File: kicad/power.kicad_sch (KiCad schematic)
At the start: 67 parts, among them J6 RTC Battery, U1 MIMXRT1171DVMAB, U8 TPS62086, U9 TPS62825, Y3 24MHz, Y4 32.768kHz

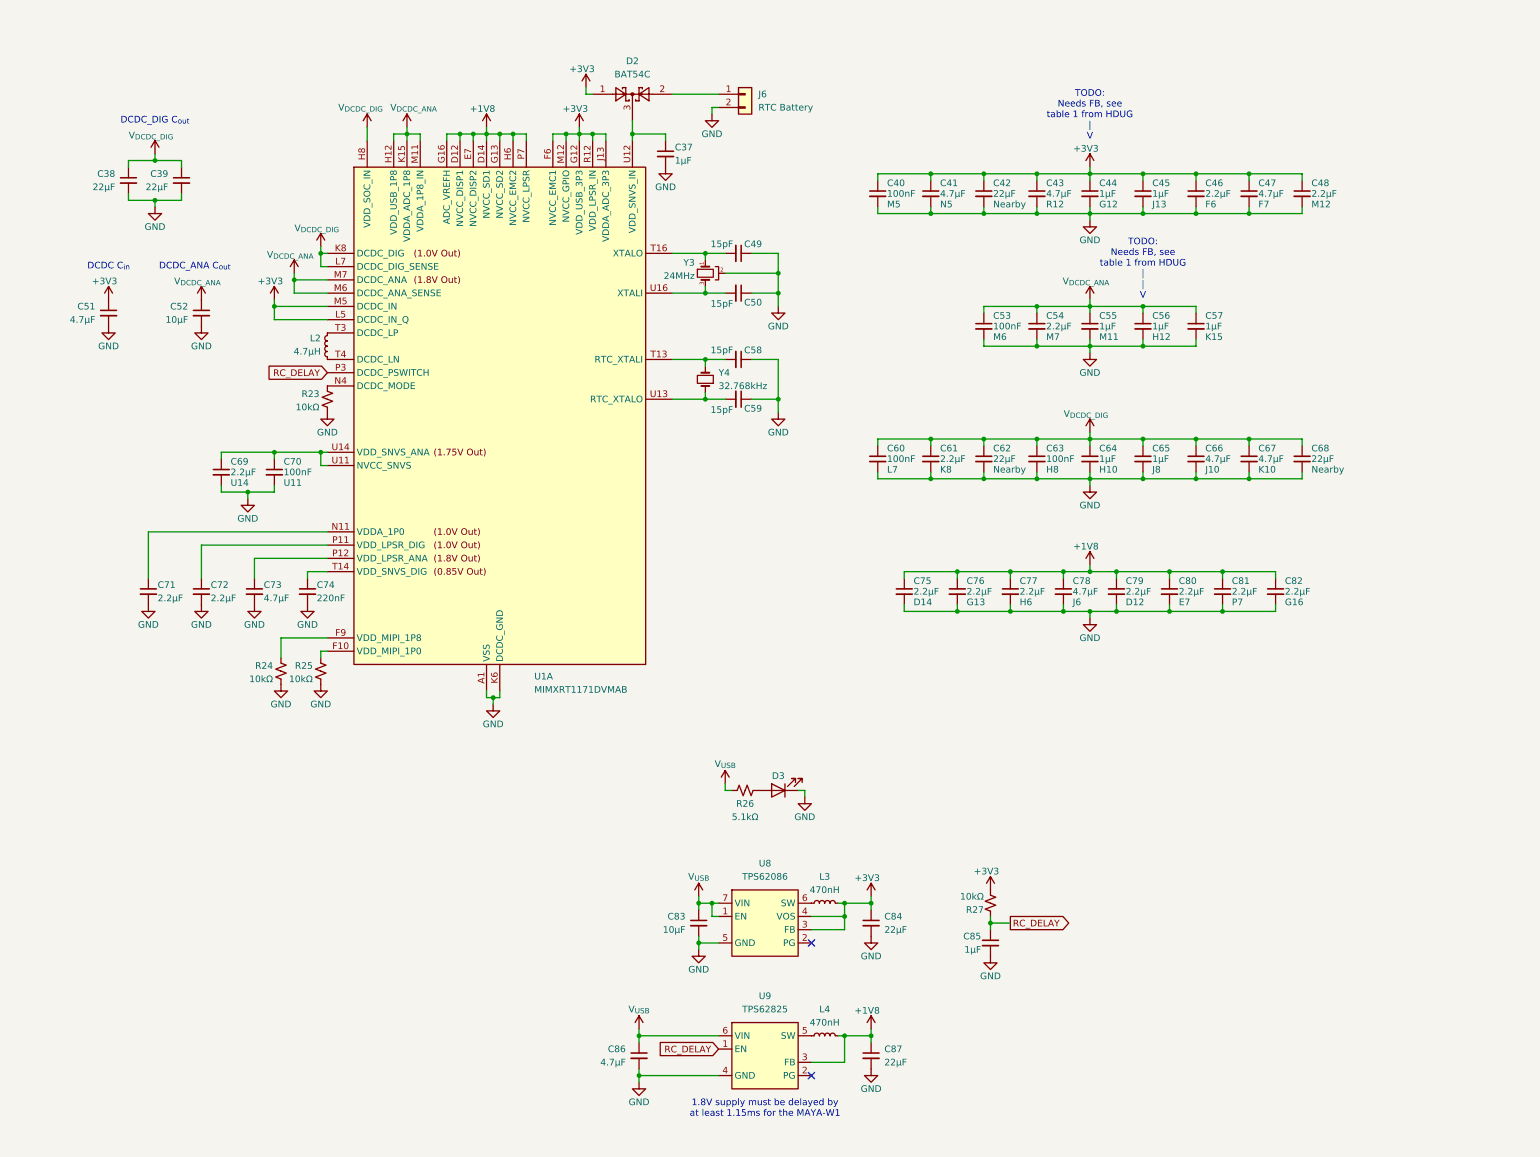
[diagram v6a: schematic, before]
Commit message: added ferrite beads to VDD_USB_xxx pins
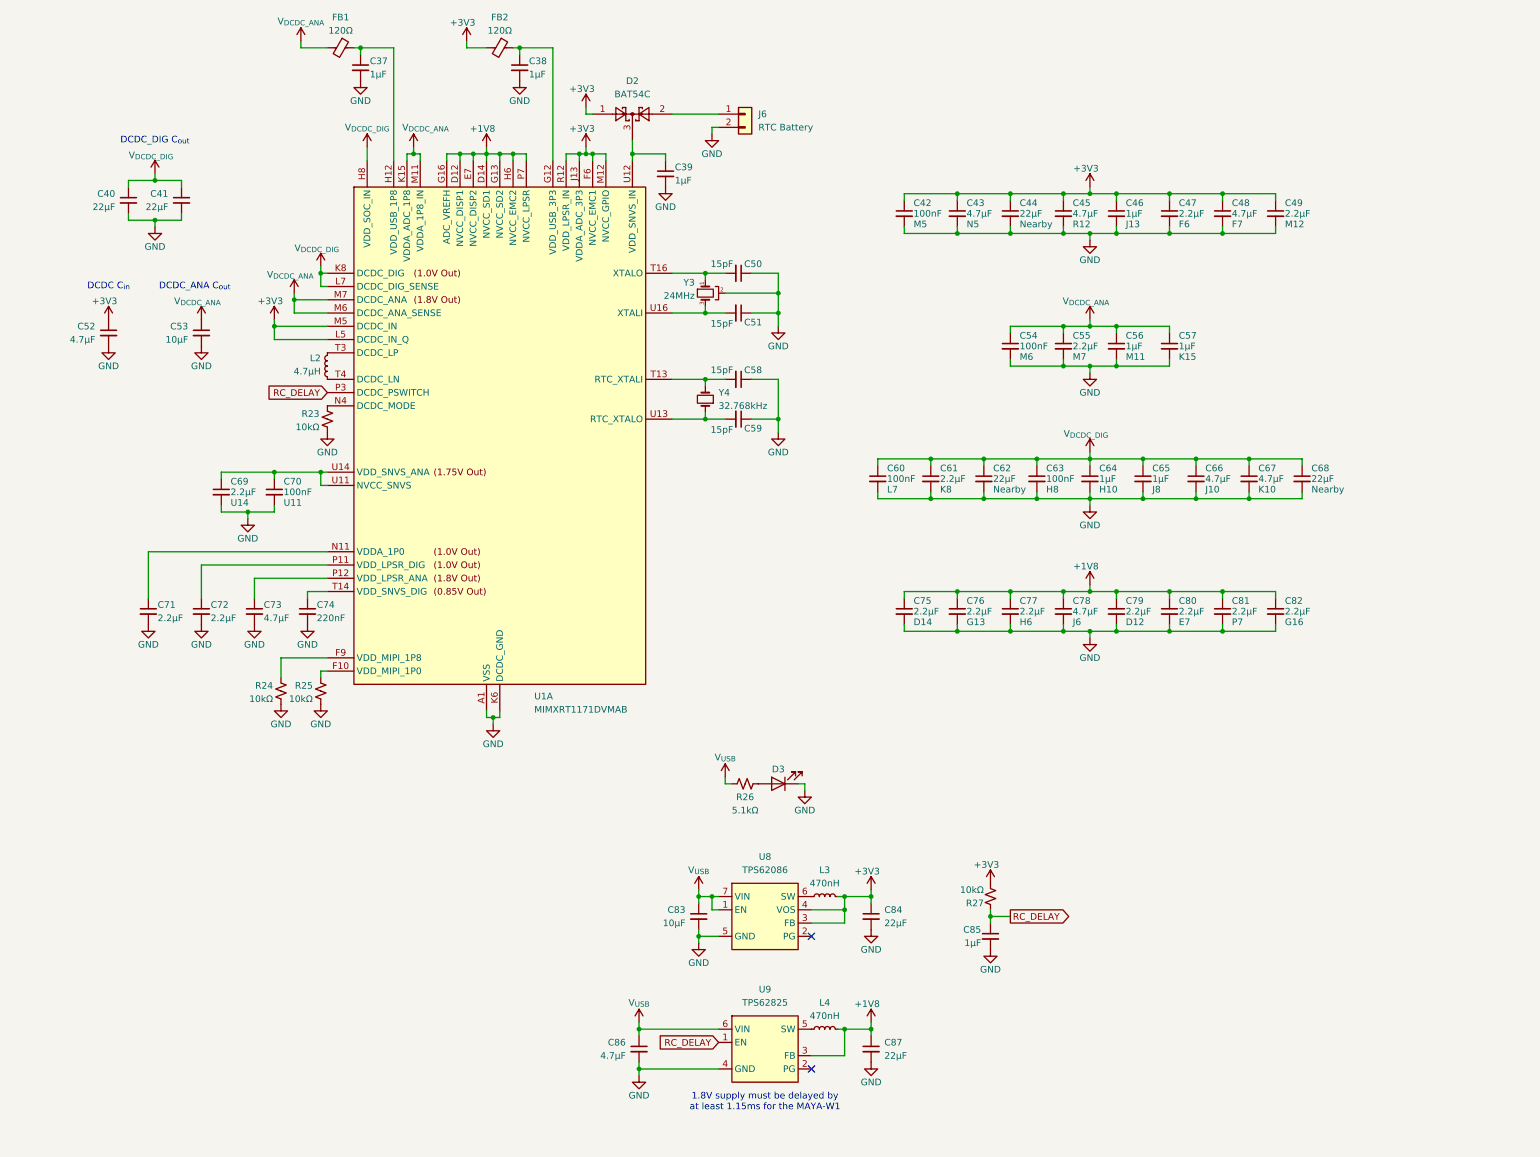
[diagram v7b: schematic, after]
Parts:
- removed C44, C56: 1μF, symbol Device:C_Small
- added C37, C38: 1μF, symbol Device:C_Small
- added FB1, FB2: 120Ω, symbol Device:FerriteBead_Small
- renumbered C37 to C39, C38 to C40, C39 to C41, C40 to C42, C41 to C43, C42 to C44, C43 to C45, C45 to C46, C46 to C47, C47 to C48, C48 to C49, C49 to C50, C50 to C51, C51 to C52, C52 to C53, C53 to C54, C54 to C55, C55 to C56
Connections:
- net +3V3: now also FB2.2; no longer U1.G12 (VDD_USB_3P3)
- net GND: now also C37.2, C38.2
- net V_{DCDC_ANA}: now also FB1.2; no longer U1.H12 (VDD_USB_1P8)
- new net: C38.1, FB2.1, U1.G12 (VDD_USB_3P3)
- new net: C37.1, FB1.1, U1.H12 (VDD_USB_1P8)
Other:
- note removed: "TODO: Needs FB, see table 1 from HDUG | V"
- note removed: "TODO: Needs FB, see table 1 from HDUG | | V"
- moved on the sheet: C39, C40, C41, C42, C43, C44, C45, C46, C47, C48, C49, C50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

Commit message: reworked USB circuitry
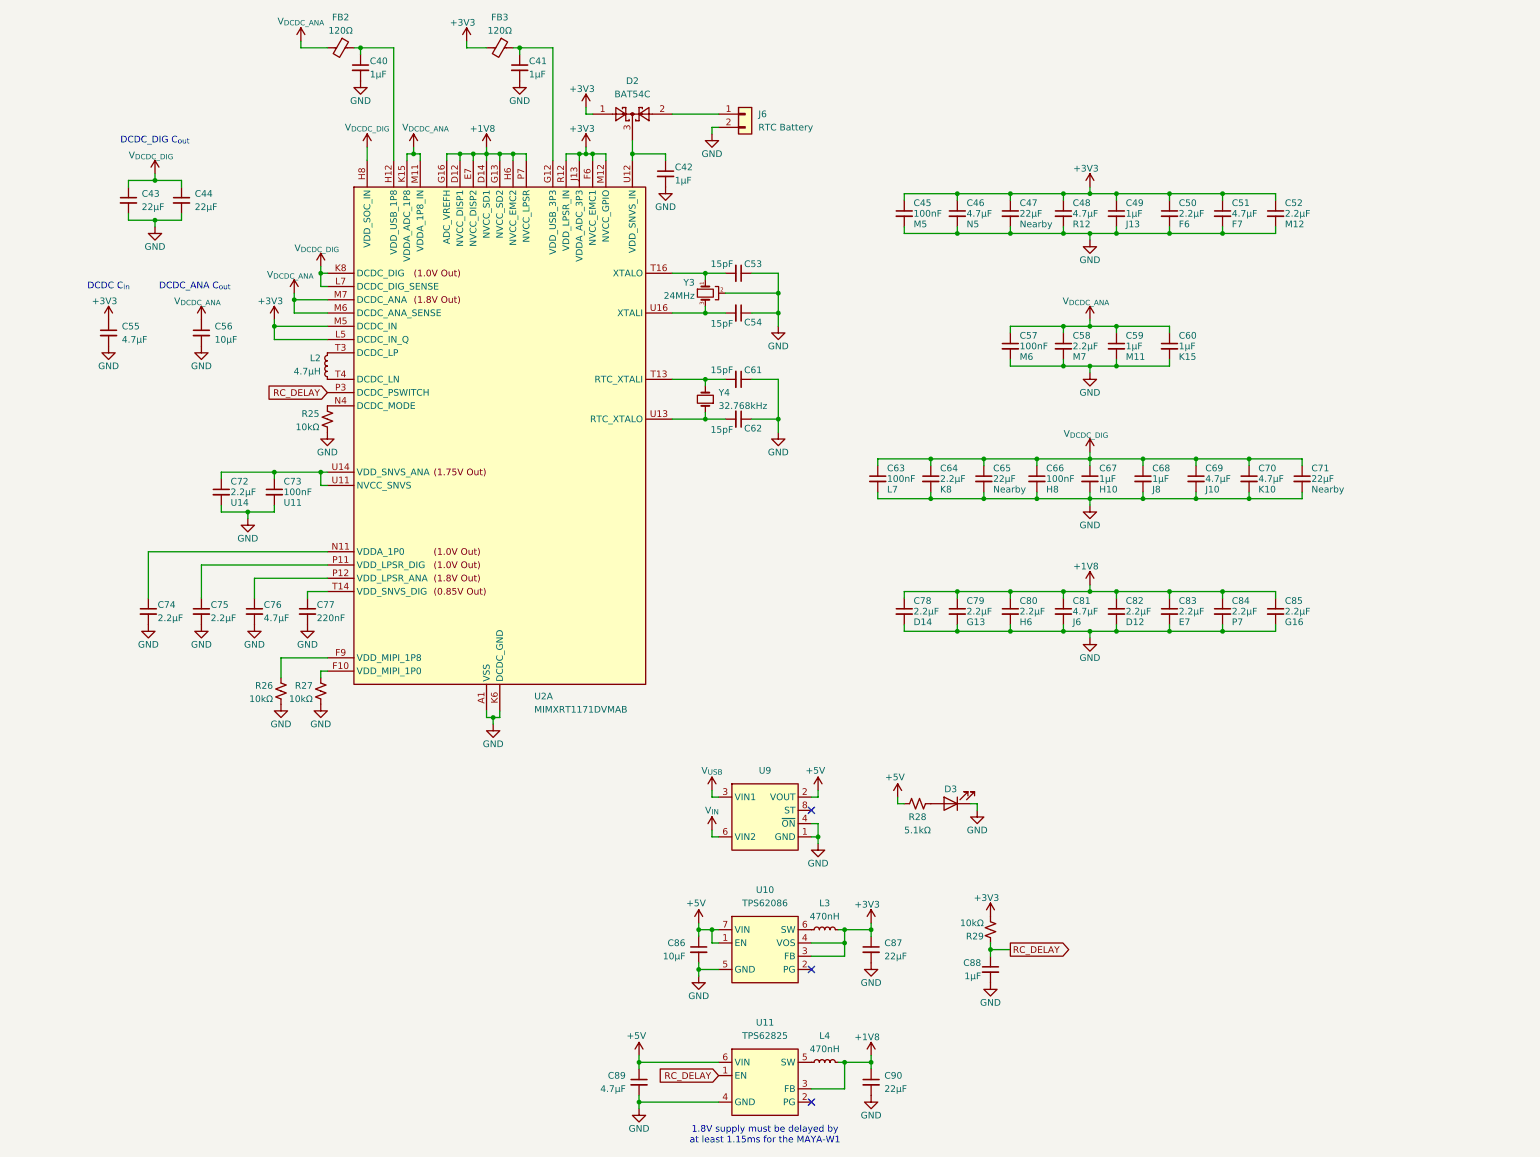
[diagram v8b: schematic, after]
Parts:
- removed R26: 5.1kΩ, Resistor_SMD:R_0201_0603Metric, symbol Device:R_Small_US
- added R28: 5.1kΩ, Resistor_SMD:R_0201_0603Metric, symbol Device:R_Small_US
- added U9: (no value), symbol project_symbols:LM66200
- renumbered C37 to C40, C38 to C41, C39 to C42, C40 to C43, C41 to C44, C42 to C45, C43 to C46, C44 to C47, C45 to C48, C46 to C49, C47 to C50, C48 to C51, C49 to C52, C50 to C53, C51 to C54, C52 to C55, C53 to C56, C54 to C57, C55 to C58, C56 to C59, C57 to C60, C58 to C61, C59 to C62, C60 to C63, C61 to C64, C62 to C65, C63 to C66, C64 to C67, C65 to C68, C66 to C69, C67 to C70, C68 to C71, C69 to C72, C70 to C73, C71 to C74, C72 to C75, C73 to C76, C74 to C77, C75 to C78, C76 to C79, C77 to C80, C78 to C81, C79 to C82, C80 to C83, C81 to C84, C82 to C85, C83 to C86, C84 to C87, C85 to C88, C86 to C89, C87 to C90, FB1 to FB2, FB2 to FB3, R23 to R25, R24 to R26, R25 to R27, R27 to R29, U8 to U10, U9 to U11, U1 to U2
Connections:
- net GND: now also U9.1 (GND), U9.4 (~{ON}), U9.5 (GND)
- net V_{USB}: now also U9.3 (VIN1); no longer C86.1, C89.1, U10.1 (EN), U10.7 (VIN), U11.6 (VIN)
- net at D3.2 (A): now also R28.2
- new net +5V: C86.1, C89.1, R28.1, U10.1 (EN), U10.7 (VIN), U11.6 (VIN), U9.2 (VOUT), U9.7 (VOUT)
- new net V_{IN}: U9.6 (VIN2)
- no-connect marks 2 -> 3
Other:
- moved on the sheet: C86, C87, C88, C89, C90, L3, L4, R29, U10, U11
